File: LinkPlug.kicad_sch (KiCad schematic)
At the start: 10 parts, among them J1901 2x05_Horizontal, U1902 SN65MLVD203B

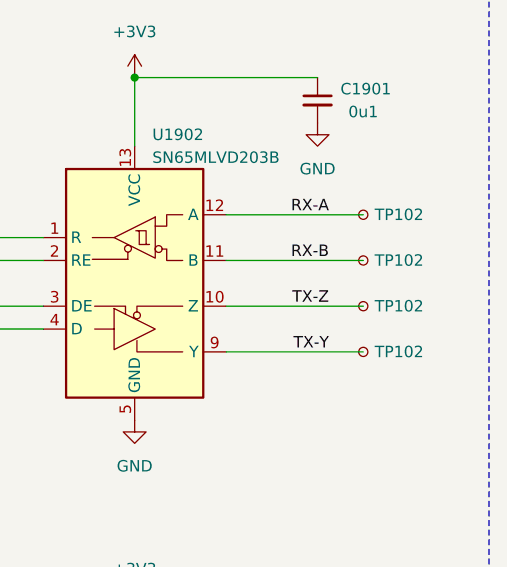
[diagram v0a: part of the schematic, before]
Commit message: Update to Kicad 8
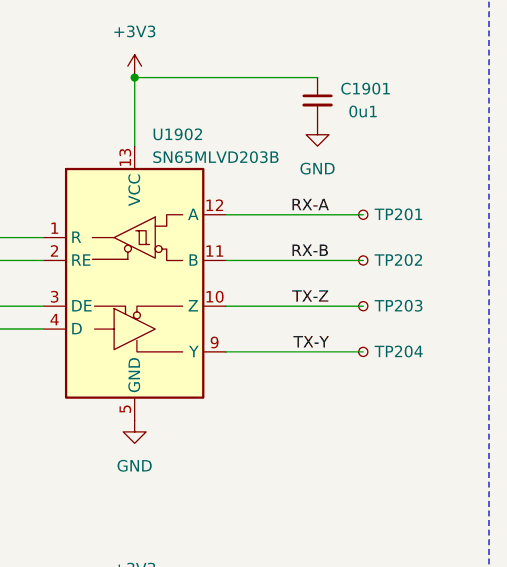
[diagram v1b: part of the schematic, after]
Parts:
- renumbered TP102 to TP201, TP102 to TP202, TP102 to TP203, TP102 to TP204
